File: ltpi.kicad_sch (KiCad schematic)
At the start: 1 part, among them J6 PinHeader_2x10_P1.27mm_SMD_Sh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

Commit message: [#93514] Propagate title and date across all of the sheets
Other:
- title: (none) -> Datacenter Secure Control Module Breakout Board
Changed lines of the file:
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@@
 	(generator_version "9.0")
 	(paper "A3")
+	(title_block
+		(title "Datacenter Secure Control Module Breakout Board")
+		(date "2021-12-16")
+		(rev "2.0.0")
+	)
 	(text "LTPI\n"
 		(exclude_from_sim no)

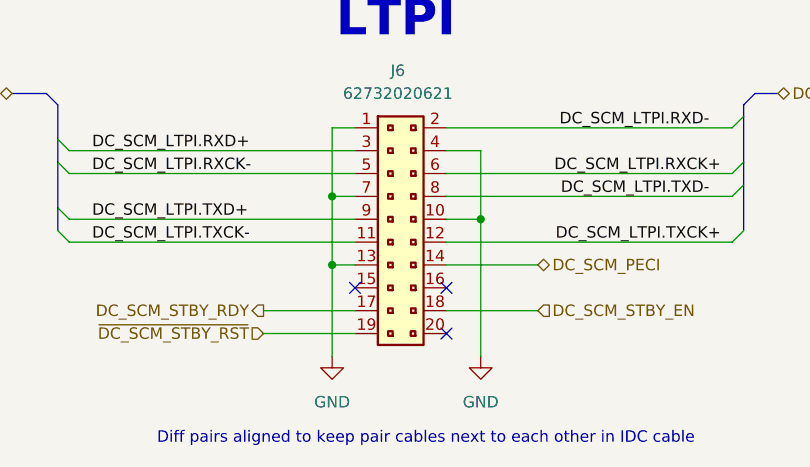
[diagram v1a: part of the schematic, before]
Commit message: [#93514] Add test pads to LPTI PECI_I2C
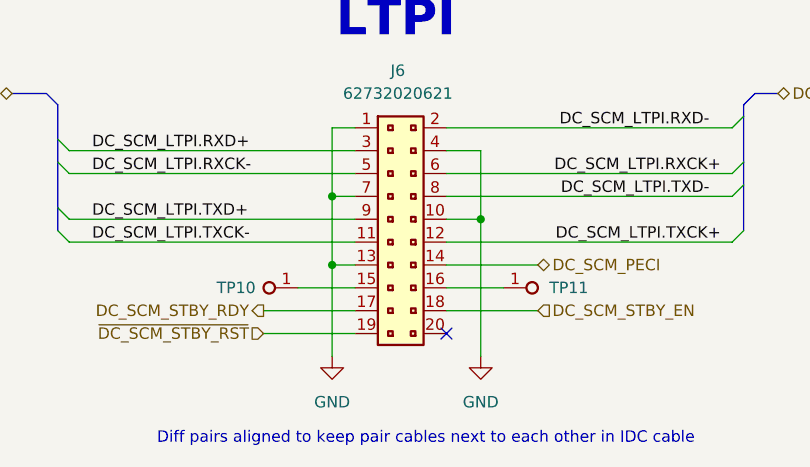
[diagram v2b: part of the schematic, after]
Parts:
- added TP10, TP11: TP_0.75mm_SMD, antmicro-footprints:TP_SMD_0.75mm, symbol antmicroTestPoints:TP_0.75mm_SMD
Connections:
- net at J6.15: now also TP10.1
- net at J6.16: now also TP11.1
- no-connect marks 3 -> 1

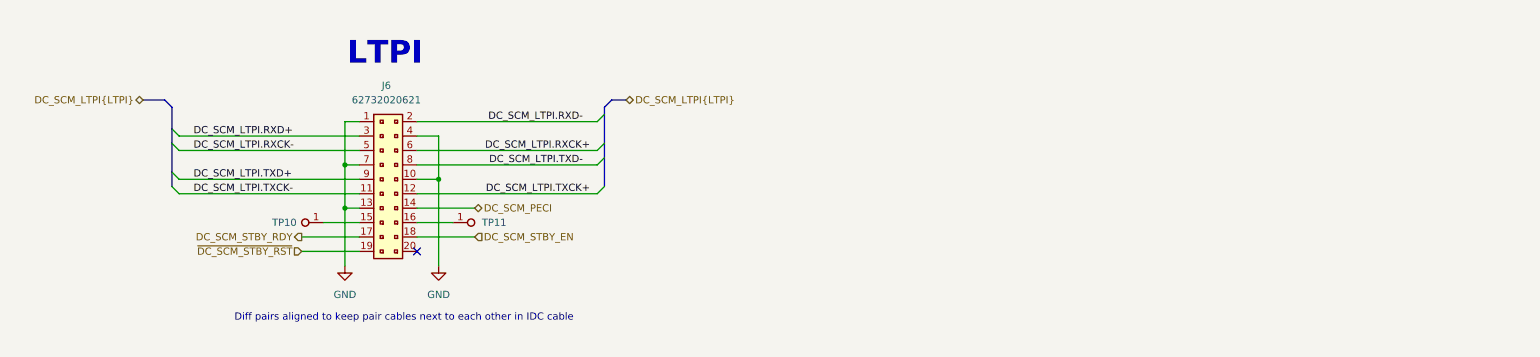
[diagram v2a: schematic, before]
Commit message: [#93514] Remove led schematic, add transistors to RST EN IRQ LEDs
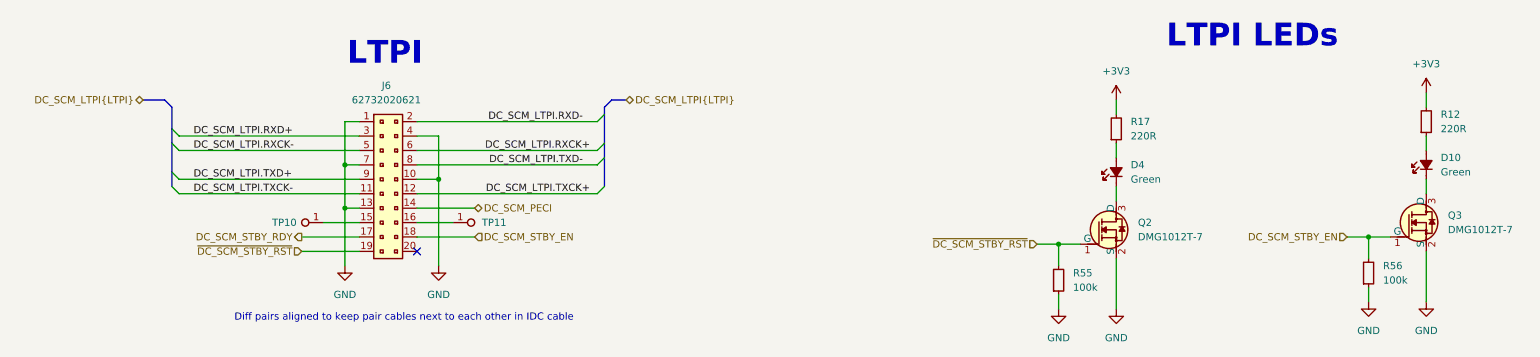
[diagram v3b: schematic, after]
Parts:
- added D10, D4: LED_G_0402_VLMTG1500-GS08, antmicro-footprints:LED_0402_1005Metric_G, symbol antmicroLEDIndicationDiscrete:LED_G_0402_VLMTG1500-GS08
- added Q2, Q3: DMG1012T-7, antmicro-footprints:SOT-523, symbol antmicroTransistorsFETsMOSFETsSingle:DMG1012T-7
- added R12, R17: R_220R_0402, antmicro-footprints:R_0402_1005Metric, symbol antmicroResistors0402:R_220R_0402
- added R55, R56: R_100k_0402, antmicro-footprints:R_0402_1005Metric, symbol antmicroResistors0402:R_100k_0402
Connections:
- net DC_SCM_STBY_EN: now also Q3.1 (G), R56.2
- net GND: now also Q2.2 (S), Q3.2 (S), R55.1, R56.1
- net ~{DC_SCM_STBY_RST}: now also Q2.1 (G), R55.2
- new net: D4.1 (C), Q2.3 (D)
- new net: D4.2 (A), R17.1
- new net: D10.1 (C), Q3.3 (D)
- new net: D10.2 (A), R12.1
- new net +3V3: R12.2, R17.2
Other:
- note added: "LTPI LEDs"
